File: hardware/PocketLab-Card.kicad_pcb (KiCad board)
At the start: 4 copper layers, 85.6 x 54 mm, 267 parts, among them J1 USB-C DATA/POWER, J2 microSD, J3 EXTERNAL 400uH LF COIL, J4 PROTECTED 1S LiPo 3.7V, J5 30-PIN 2.54mm DUPONT GRID, J8 ER-OLED0.42-1W 72x40 SSD1306B, Q1 AO3400A IR DRIVER, Q2 CSD16406Q3 DISCHARGE, Q3 CSD16406Q3 CHARGE, SW1 RESET, SW2 BOOT, SW3 UP, SW4 DOWN, SW5 MAIN POWER OFF / ON, SW6 PAIR, SW7 SELECT, U1 ESP32-S3-WROOM-1-N8R2, U10 BMI270 (FULL OPTION), U11 BMP390 (FULL OPTION), U12 PCF8563T, U13 TSOP75338WTR 38kHz, U14 BQ29700DSE, U15 TPS2553DBVR 500mA LIMIT, U16 USBLC6-4SC6Y, U17 TPS22919DCKR LF 5V LOAD SWITCH, U18 TCA9534PWR INTERNAL CONTROL, U19 SRV05-4MR6T1G SD ESD, U2 PN5321A3HN/C106, U20 SN74AHCT1G126DBVR RGB LEVEL S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, U21 SN74LV125ATPWR LF/SPI 3V3-TO-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, U22 SN74LVC1G126DBVR LF 5V-TO-3V3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, U23 ATECC608C-SSHDA-T, U24 SRV05-4MR6T1G J5 BUS ESD, U25 SRV05-4MR6T1G J5 SPI ESD, U3 E07-900MM10S 855-925MHz, U4 HTRC11001T/03EE,11 125kHz, U5 BQ24074RGTR, U6 TPS63070RNMR 3V3, U7 TPS61023DRLR 5V BOOST, U8 MAX17048G+T10, U9 TCA9535PWR, Y301 27.12MHz crystal (pins 2/4 sh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, Y501 4MHz 5V CMOS OSCILLATOR, Y701 32.768kHz CL=7pF

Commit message: Clear OLED routing drill violations
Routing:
- net /CHARGER_PGOOD_N: track 35.5 -> 54.3 mm
- net /+3V3: track 302.6 -> 317.6 mm, vias 69 -> 70
- net /VSYS: track 58.5 -> 73.3 mm
- net /SPI_MISO_HDR: track 47.6 -> 61.9 mm
- net /USER_BUTTON_A_N: track 52.4 -> 62.8 mm
- net /I2C_SDA: track 122.7 -> 132.3 mm
- net /I2C_SCL: track 128.2 -> 137.8 mm
- net /EX4: track 47.7 -> 52.5 mm
- net /CHG_TS_FIXED: track 22.0 -> 26.8 mm
- net /+5V_RAW: track 118.0 -> 122.5 mm
- net /CELL_POS: track 52.9 -> 56.9 mm
- net /EX7: track 50.8 -> 54.8 mm
- net /EX6: track 49.0 -> 53.0 mm
- net /CHG_TS: track 40.0 -> 44.0 mm
- net /BQ_EN1: track 47.3 -> 51.3 mm
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
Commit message: Relocate congested routing vias
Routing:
- net /GND: track 415.4 -> 426.0 mm
- net /SPI_MISO: track 80.7 -> 83.9 mm
- net /SD_DETECT_N: track 67.7 -> 70.9 mm
- net /SD_MOSI: track 50.0 -> 53.2 mm
- net /CHG_TS_FIXED: track 26.8 -> 29.2 mm
- net /LF_5V: track 113.5 -> 115.9 mm
- net /CHG_DISABLE: track 30.0 -> 31.6 mm
- net /USER_BUTTON_B_N: track 44.6 -> 46.2 mm
- net /VSYS: track 73.3 -> 74.9 mm
- net /IR_RX: track 44.8 -> 45.6 mm

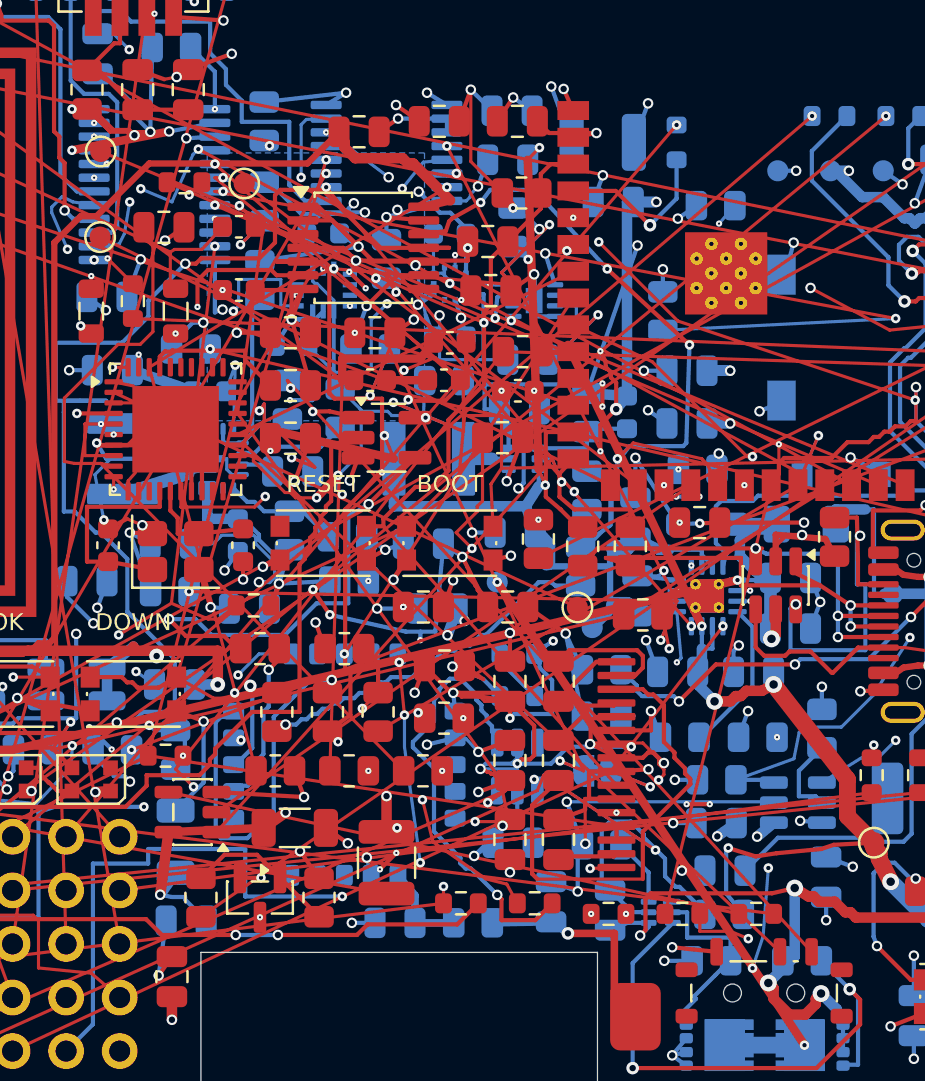
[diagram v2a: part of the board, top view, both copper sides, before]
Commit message: Relieve additional via routing conflicts
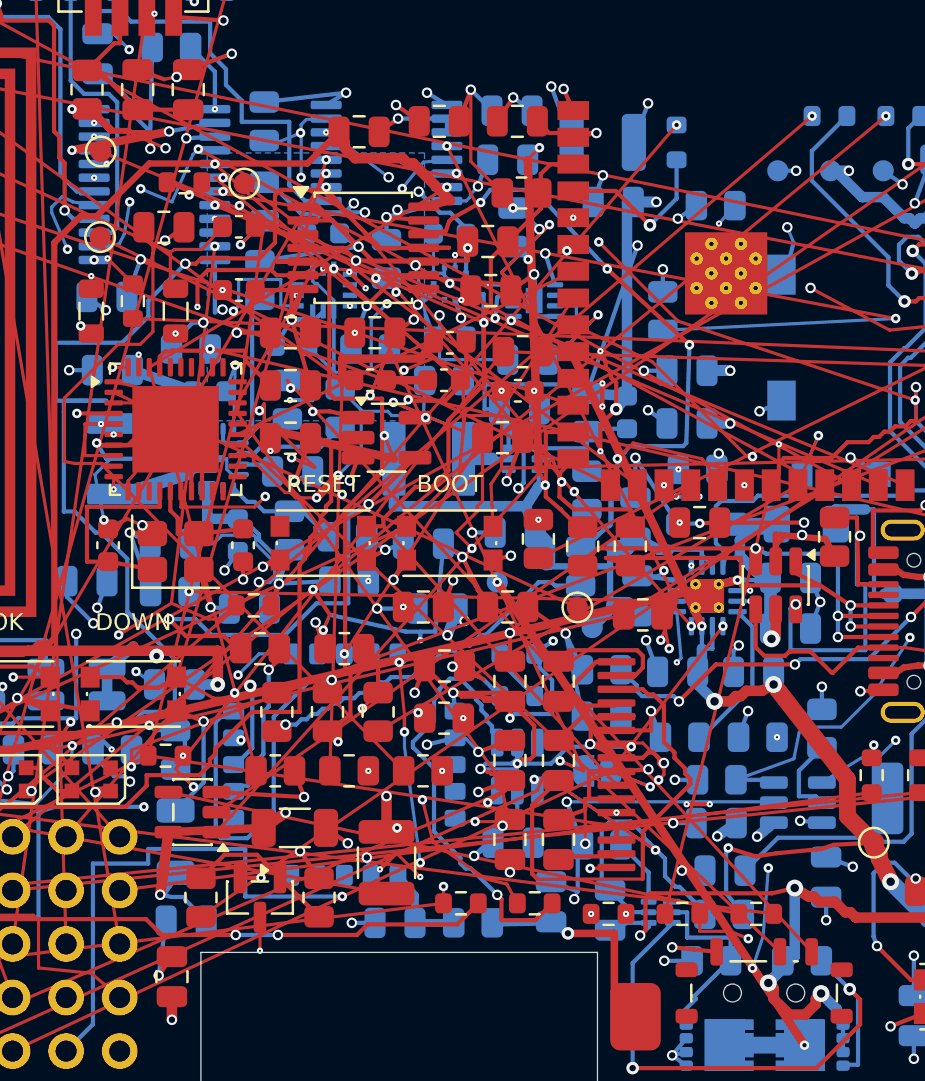
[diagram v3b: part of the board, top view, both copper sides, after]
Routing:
- net /I2C_SDA: track 132.3 -> 137.1 mm
- net /+3V3: track 317.6 -> 322.4 mm
- net /IR_LED_K: track 58.0 -> 61.1 mm
- net /GND: track 426.0 -> 428.8 mm
- net /SD_DAT2: track 44.5 -> 46.1 mm
- net /SUBGHZ_GDO2: track 72.8 -> 74.4 mm
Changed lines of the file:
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@@
 	)
 	(via micro
-		(at 69 65.7375)
+		(at 69 67.325)
 		(size 0.3)
 		(drill 0.1)
@@
 	)
 	(via
-		(at 84.063886 64.510017)
+		(at 83.9 64.875)
 		(size 0.5)
 		(drill 0.3)
@@
 	)
 	(via
-		(at 94.299959 33.751799)
+		(at 94 33.025)
 		(size 0.5)
 		(drill 0.3)
@@
 	)
 	(via micro
-		(at 75.464 62.686)
+		(at 76.6 63.825)
 		(size 0.3)
 		(drill 0.1)
@@
 	)
 	(via
-		(at 72.3125 51.395)
+		(at 72 52.125)
 		(size 0.45)
 		(drill 0.2)
@@
 	)
 	(via
-		(at 63.8 28.5)
+		(at 63.8 29.3)
 		(size 0.5)
 		(drill 0.3)
@@
 	)
 	(via
-		(at 63.05 28.6625)
+		(at 64.525 29.275)
 		(size 0.5)
 		(drill 0.3)
@@
 	)
 	(via
-		(at 69.45 29.1625)
+		(at 70.925 28.55)
 		(size 0.45)
 		(drill 0.2)
@@
 	)
 	(via
-		(at 75.85 56.15)
+		(at 75.85 56.95)
 		(size 0.45)
 		(drill 0.2)
@@
 	)
 	(via
-		(at 62.9125 57.8)
+		(at 62.9 58.6)
 		(size 0.45)
 		(drill 0.2)
@@
 		(net "/GND")
 	)
+	(segment
+		(start 75.85 56.15)
+		(end 75.85 56.95)
+		(width 0.15)
+		(locked yes)
+		(layer "F.Cu")
+		(net "/SUBGHZ_GDO2")
+	)
+	(segment
+		(start 63.8 28.5)
+		(end 63.8 29.3)
+		(width 0.15)
+		(locked yes)
+		(layer "F.Cu")
+		(net "/+3V3")
+	)
+	(segment
+		(start 69.45 29.1625)
+		(end 70.925 28.55)
+		(width 0.15)
+		(locked yes)
+		(layer "B.Cu")
+		(net "/I2C_SDA")
+	)
+	(segment
+		(start 62.9125 57.8)
+		(end 62.9 58.6)
+		(width 0.15)
+		(locked yes)
+		(layer "F.Cu")
+		(net "/SD_DAT2")
+	)
+	(segment
+		(start 69 65.7375)
+		(end 69 67.325)
+		(width 0.15)
+		(locked yes)
+		(layer "In1.Cu")
+		(net "/IR_LED_K")
+	)
+	(segment
+		(start 63.05 28.6625)
+		(end 64.525 29.275)
+		(width 0.15)
+		(locked yes)
+		(layer "F.Cu")
+		(net "/+3V3")
+	)
+	(segment
+		(start 75.85 56.15)
+		(end 75.85 56.95)
+		(width 0.15)
+		(locked yes)
+		(layer "B.Cu")
+		(net "/SUBGHZ_GDO2")
+	)
+	(segment
+		(start 84.063886 64.510017)
+		(end 83.9 64.875)
+		(width 0.15)
+		(locked yes)
+		(layer "B.Cu")
+		(net "/GND")
+	)
+	(segment
+		(start 69.45 29.1625)
+		(end 70.925 28.55)
+		(width 0.15)
+		(locked yes)
+		(layer "In1.Cu")
+		(net "/I2C_SDA")
+	)
+	(segment
+		(start 62.9125 57.8)
+		(end 62.9 58.6)
+		(width 0.15)
+		(locked yes)
+		(layer "B.Cu")
+		(net "/SD_DAT2")
+	)
+	(segment
+		(start 69.45 29.1625)
+		(end 70.925 28.55)
+		(width 0.15)
+		(locked yes)
+		(layer "In2.Cu")
+		(net "/I2C_SDA")
+	)
+	(segment
+		(start 72.3125 51.395)
+		(end 72 52.125)
+		(width 0.15)
+		(locked yes)
+		(layer "F.Cu")
+		(net "/+3V3")
+	)
+	(segment
+		(start 75.464 62.686)
+		(end 76.6 63.825)
+		(width 0.15)
+		(locked yes)
+		(layer "F.Cu")
+		(net "/GND")
+	)
+	(segment
+		(start 63.8 28.5)
+		(end 63.8 29.3)
+		(width 0.15)
+		(locked yes)
+		(layer "B.Cu")
+		(net "/+3V3")
+	)
+	(segment
+		(start 72.3125 51.395)
+		(end 72 52.125)
+		(width 0.15)
+		(locked yes)
+		(layer "B.Cu")
+		(net "/+3V3")
+	)
+	(segment
+		(start 94.299959 33.751799)
+		(end 94 33.025)
+		(width 0.15)
+		(locked yes)
+		(layer "B.Cu")
+		(net "/GND")
+	)
+	(segment
+		(start 69 65.7375)
+		(end 69 67.325)
+		(width 0.15)
+		(locked yes)
+		(layer "F.Cu")
+		(net "/IR_LED_K")
+	)
 	(zone

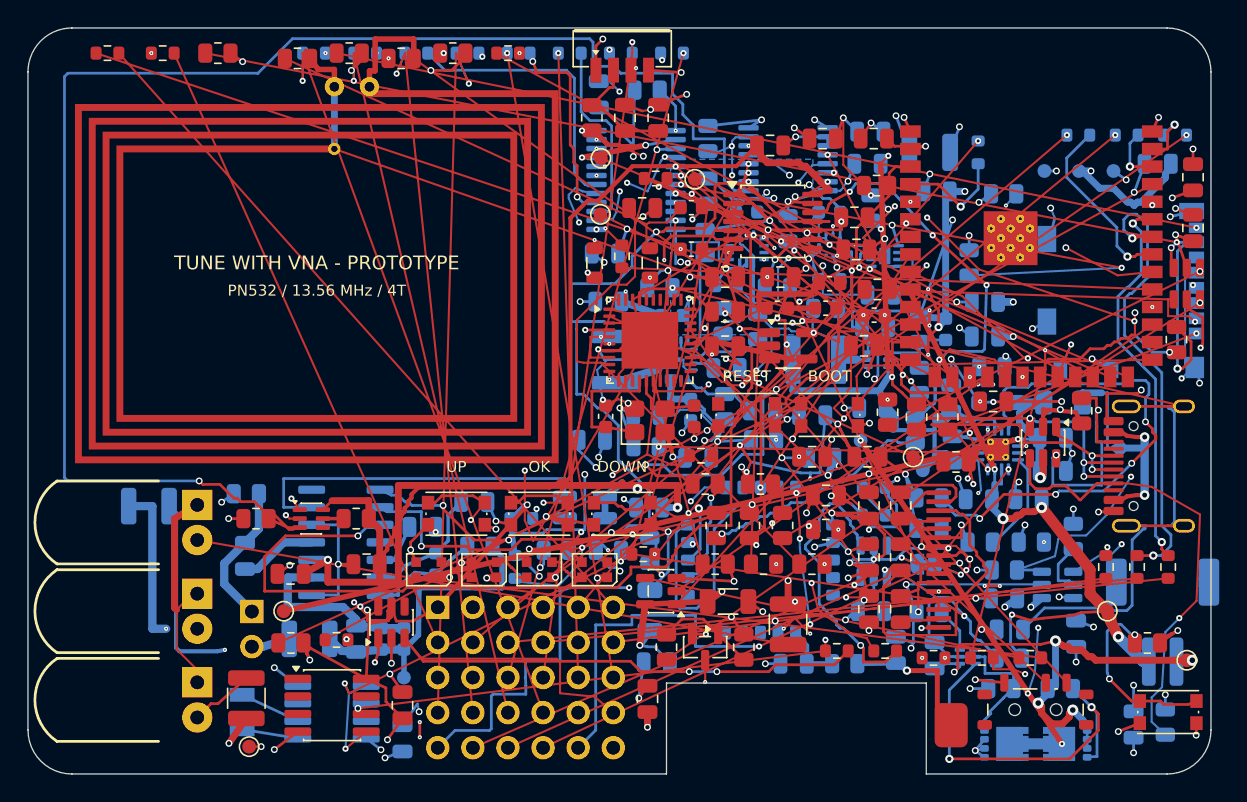
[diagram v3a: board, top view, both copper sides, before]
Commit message: Publish current routing checkpoint and 3D viewer
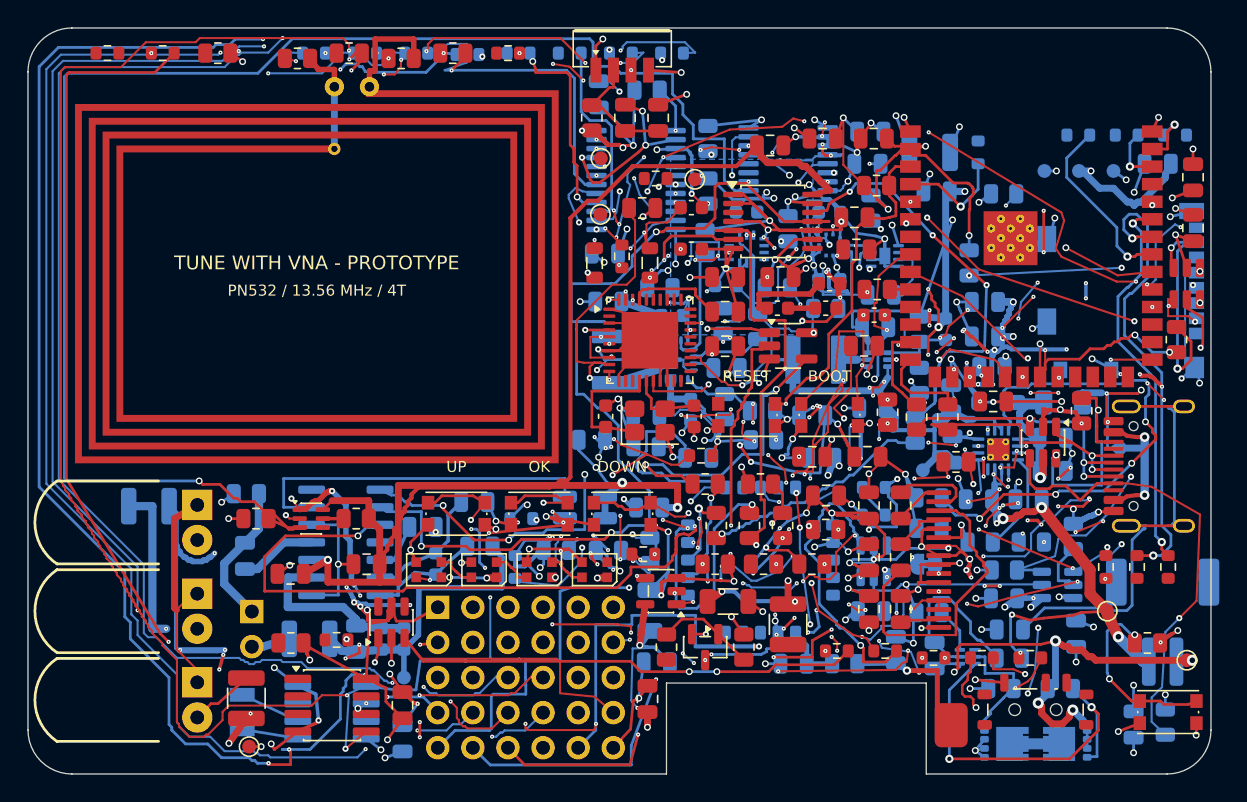
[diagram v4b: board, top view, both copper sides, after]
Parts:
- removed TP103: BATTERY BAT_FET_MID, TestPoint:TestPoint_Pad_D1.0mm
- removed TP106: POWER VBUS_FUSED, TestPoint:TestPoint_Pad_D1.0mm
- removed TP301: NFC_LOADMOD TEST, TestPoint:TestPoint_Pad_D1.0mm
- moved R726 0.10 mm to (51.8, 21.9)
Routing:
- net /+5V_RAW: track 122.5 -> 304.8 mm, vias 28 -> 67
- net /GND: track 428.8 -> 607.0 mm, vias 145 -> 213
- net /+3V3: track 322.4 -> 427.1 mm, vias 70 -> 102
- net /EX1: track 47.2 -> 127.9 mm, vias 1 -> 9
- net /EX0: track 46.9 -> 121.6 mm, vias 1 -> 6
- net /SD_MISO: track 89.7 -> 18.0 mm, vias 3 -> 2
- net /GPIO43_MCU: track 68.3 -> 0.00 mm
- net /+5V_AUX: track 36.9 -> 104.0 mm, vias 5 -> 9
- net /SD_DAT1: track 63.5 -> 0.00 mm, vias 1 -> 0
- net /EX4: track 52.5 -> 114.8 mm, vias 1 -> 11
- net /GPIO8_MCU: track 62.1 -> 0.00 mm
- net /BOOST5_EN: track 52.3 -> 112.2 mm, vias 3 -> 28
- net /GPIO1: track 59.8 -> 0.00 mm, vias 1 -> 0
- net /GPIO40: track 56.5 -> 0.00 mm, vias 1 -> 0
- net /VBUS_FUSED: track 67.1 -> 12.5 mm, vias 2 -> 1
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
